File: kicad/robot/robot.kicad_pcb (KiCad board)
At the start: 4 copper layers, 3 parts

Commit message: initial layout work
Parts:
- removed ZZ1: These assemblies are ESD sensitive, ESD precautions shall b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, AltiumImports:AssemblyNote
- removed ZZ2: These assemblies must be clean and free from flux and all c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, AltiumImports:AssemblyNote
- removed ZZ3: These assemblies must comply with workmanship standards IPC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, AltiumImports:AssemblyNote
- added BT1: DNP, custom_modules:battery26650_thermistor, F.Cu at (100.1, 74.9)
- added C1: 100uF, Capacitor_SMD:C_1210_3225Metric, F.Cu at (233.3, 101.4)
- added C10: 1u, Capacitor_SMD:C_0402_1005Metric, F.Cu at (87.9, 139.6)
- added C11: 100n, Capacitor_SMD:C_0402_1005Metric, F.Cu at (79.0, 146.1)
- added C12: 100n, Capacitor_SMD:C_0402_1005Metric, F.Cu at (91.2, 142.5)
- added C13: 100n, Capacitor_SMD:C_0402_1005Metric, F.Cu at (91.2, 146.6)
- added C14: 100n, Capacitor_SMD:C_0402_1005Metric, F.Cu at (84.4, 151.3)
- added C15: 100n, Capacitor_SMD:C_0402_1005Metric, F.Cu at (79.0, 142.5)
- added C16: 100n, Capacitor_SMD:C_0402_1005Metric, F.Cu at (88.9, 139.6)
- added C17: 10u, Capacitor_SMD:C_0603_1608Metric, F.Cu at (78.5, 147.3)
- added C18: 27pF, Capacitor_SMD:C_0402_1005Metric, F.Cu at (128.7, 105.5)
- added C19: 27pF, Capacitor_SMD:C_0402_1005Metric, F.Cu at (128.7, 104.5)
- added C2: 27p, Capacitor_SMD:C_0402_1005Metric, F.Cu at (74.3, 158.3)
- added C20: 2.2uF, Capacitor_SMD:C_0805_2012Metric, F.Cu at (123.2, 108.1)
- added C21: 1uF, Capacitor_SMD:C_0805_2012Metric, F.Cu at (94.7, 98.2)
- added C22: 1uF, Capacitor_SMD:C_0805_2012Metric, F.Cu at (98.2, 100.0)
- added C23: 4.7uF, Capacitor_SMD:C_0805_2012Metric, F.Cu at (101.5, 98.2)
- added C24: 100nF, Capacitor_SMD:C_0603_1608Metric, F.Cu at (80.9, 115.8)
- added C25: 10uF, Capacitor_SMD:C_0805_2012Metric, F.Cu at (86.1, 116.1)
- added C26: 0.47uF, Capacitor_SMD:C_0603_1608Metric, F.Cu at (83.4, 118.0)
- added C27: 10uF, Capacitor_SMD:C_0805_2012Metric, F.Cu at (88.1, 116.1)
- added C28: 2.2uF, Capacitor_SMD:C_0603_1608Metric, F.Cu at (83.4, 122.5)
- added C29: 100nF, Capacitor_SMD:C_0805_2012Metric, F.Cu at (90.2, 116.1)
- added C3: 27p, Capacitor_SMD:C_0402_1005Metric, F.Cu at (82.4, 158.3)
- added C30: 0.22uF, Capacitor_SMD:C_0603_1608Metric, F.Cu at (92.4, 118.9)
- added C31: 0.22uF, Capacitor_SMD:C_0603_1608Metric, F.Cu at (92.4, 121.9)
- added C32: 100nF, Capacitor_SMD:C_0805_2012Metric, F.Cu at (86.1, 124.6)
- added C33: 22uF, Capacitor_SMD:C_0805_2012Metric, F.Cu at (88.1, 124.6)
- added C34: 22uF, Capacitor_SMD:C_0805_2012Metric, F.Cu at (90.2, 124.6)
- added C35: 0.1uF, Capacitor_SMD:C_0603_1608Metric, F.Cu at (96.4, 147.4)
- added C36: 100nF, Capacitor_SMD:C_0603_1608Metric, F.Cu at (91.7, 145.3)
- added C37: 100nF, Capacitor_SMD:C_0603_1608Metric, F.Cu at (94.1, 139.3)
- added C38: 100nF, Capacitor_SMD:C_0603_1608Metric, F.Cu at (101.0, 141.5)
- added C39: 100nF, Capacitor_SMD:C_0603_1608Metric, F.Cu at (101.0, 146.1)
- added C4: 1uF, Capacitor_SMD:C_0603_1608Metric, F.Cu at (64.0, 118.4)
- added C40: 100nF, Capacitor_SMD:C_0805_2012Metric, F.Cu at (120.5, 123.0)
- added C41: 100nF, Capacitor_SMD:C_0805_2012Metric, F.Cu at (131.3, 123.8)
- added C42: 10uF, Capacitor_SMD:C_0805_2012Metric, F.Cu at (120.5, 120.9)
- added C43: 10uF, Capacitor_SMD:C_0805_2012Metric, F.Cu at (131.3, 125.8)
- added C44: 0.1uF, Capacitor_SMD:C_0603_1608Metric, F.Cu at (133.0, 129.9)
- added C45: 27pF, Capacitor_SMD:C_0402_1005Metric, B.Cu at (156.6, 149.4)
- added C46: 27pF, Capacitor_SMD:C_0402_1005Metric, B.Cu at (155.6, 149.4)
- added C47: 1uF, Capacitor_SMD:C_0805_2012Metric, F.Cu at (156.1, 147.5)
- added C48: 1uF, Capacitor_SMD:C_0805_2012Metric, F.Cu at (162.5, 152.4)
- added C49: 2.2uF, Capacitor_SMD:C_0603_1608Metric, F.Cu at (162.3, 154.2)
- added C5: 100n, Capacitor_SMD:C_0402_1005Metric, F.Cu at (80.6, 130.8)
- added C50: 1uF, Capacitor_SMD:C_0805_2012Metric, F.Cu at (159.6, 147.5)
- added C51: 1uF, Capacitor_SMD:C_0603_1608Metric, F.Cu at (154.3, 147.8)
- added C52: 1uF, Capacitor_SMD:C_0603_1608Metric, F.Cu at (157.9, 147.7)
- added C53: 1uF, Capacitor_SMD:C_0603_1608Metric, F.Cu at (149.7, 152.5)
- added C54: 1uF, Capacitor_SMD:C_0603_1608Metric, F.Cu at (149.8, 150.9)
- added C55: 1uF, Capacitor_SMD:C_0603_1608Metric, F.Cu at (66.4, 105.9)
- added C56: 0.47uF, Capacitor_SMD:C_0603_1608Metric, F.Cu at (68.0, 105.9)
- added C57: 0.1uF, Capacitor_SMD:C_0603_1608Metric, F.Cu at (62.9, 103.2)
- added C58: 0.1uF, Capacitor_SMD:C_0603_1608Metric, F.Cu at (62.9, 100.1)
- added C59: 0.1uF, Capacitor_SMD:C_0603_1608Metric, F.Cu at (64.7, 95.8)
- added C6: 100n, Capacitor_SMD:C_0402_1005Metric, F.Cu at (84.9, 139.6)
- added C60: 0.1uF, Capacitor_SMD:C_0603_1608Metric, F.Cu at (67.0, 96.6)
- added C61: 0.1uF, Capacitor_SMD:C_0603_1608Metric, F.Cu at (69.3, 95.8)
- added C62: 0.1uF, Capacitor_SMD:C_0603_1608Metric, F.Cu at (71.0, 93.2)
- added C63: 0.1uF, Capacitor_SMD:C_0603_1608Metric, F.Cu at (72.5, 93.2)
- added C64: 0.1uF, Capacitor_SMD:C_0603_1608Metric, F.Cu at (72.1, 104.2)
- added C65: 0.1uF, Capacitor_SMD:C_0603_1608Metric, F.Cu at (76.0, 96.9)
- added C66: 0.1uF, Capacitor_SMD:C_0603_1608Metric, F.Cu at (76.0, 100.0)
- added C67: 10uF, Capacitor_SMD:C_0805_2012Metric, F.Cu at (123.2, 143.5)
- added C68: 10uF, Capacitor_SMD:C_0805_2012Metric, F.Cu at (123.2, 141.4)
- added C69: 1uF, Capacitor_SMD:C_0603_1608Metric, F.Cu at (118.8, 157.6)
- added C7: 100n, Capacitor_SMD:C_0402_1005Metric, F.Cu at (85.4, 151.3)
- added C70: 100nF, Capacitor_SMD:C_0603_1608Metric, F.Cu at (117.3, 157.6)
- added C71: 100nF, Capacitor_SMD:C_0603_1608Metric, F.Cu at (117.7, 147.6)
- added C72: 100nF, Capacitor_SMD:C_0603_1608Metric, F.Cu at (111.6, 151.9)
- added C73: 100nF, Capacitor_SMD:C_0603_1608Metric, F.Cu at (122.1, 152.5)
- added C74: 100nF, Capacitor_SMD:C_0603_1608Metric, F.Cu at (72.2, 119.9)
- added C75: 10uF, Capacitor_SMD:C_0603_1608Metric, F.Cu at (111.5, 153.5)
- added C76: 22uF, Capacitor_SMD:C_0805_2012Metric, F.Cu at (125.5, 152.3)
- added C77: 10uF, Capacitor_SMD:C_0805_2012Metric, F.Cu at (122.0, 150.6)
- added C78: 22uF, Capacitor_SMD:C_0805_2012Metric, F.Cu at (125.5, 150.2)
- added C8: 1u, Capacitor_SMD:C_0402_1005Metric, F.Cu at (86.9, 139.6)
- added C80: 10uF, Capacitor_SMD:C_0805_2012Metric, F.Cu at (122.0, 148.5)
- added C84: 10nF, Capacitor_SMD:C_0402_1005Metric, F.Cu at (69.3, 121.5)
- added C85: 100nF, Capacitor_SMD:C_0603_1608Metric, F.Cu at (64.0, 121.4)
- added C86: 22uF, Capacitor_SMD:C_0603_1608Metric, F.Cu at (72.2, 121.4)
- added C87: 22uF, Capacitor_SMD:C_0603_1608Metric, F.Cu at (64.0, 119.9)
- added C88: 1uF, Capacitor_SMD:C_0603_1608Metric, F.Cu at (72.0, 114.5)
- added C9: 100n, Capacitor_SMD:C_0402_1005Metric, F.Cu at (86.0, 139.6)
- added C90: 100nF, Capacitor_SMD:C_0603_1608Metric, F.Cu at (72.2, 116.9)
- added C91: 22uF, Capacitor_SMD:C_0603_1608Metric, F.Cu at (72.2, 118.4)
- added C92: 100nF, Capacitor_SMD:C_0603_1608Metric, F.Cu at (70.5, 114.5)
- added C93: 22uF, Capacitor_SMD:C_0603_1608Metric, F.Cu at (69.0, 114.5)
- added C94: 100uF, Capacitor_SMD:C_1210_3225Metric, F.Cu at (125.9, 108.6)
- added D1: AZ23C5V6-7-F, Package_TO_SOT_SMD:Diodes_Inc-SOT23-01_2017-0-MFG, F.Cu at (134.2, 95.1)
- added D2: PTVS20VS1UR, Diode_SMD:Nexperia_CFP3_SOD-123W, F.Cu at (128.7, 108.6)
- added D5: PTVS20VS1UR, Diode_SMD:Nexperia_CFP3_SOD-123W, F.Cu at (123.8, 145.6)
- added D6: LED, Diode_SMD:D_0603_1608Metric_Harvatek, F.Cu at (114.7, 144.5)
- added H1: MountingHole, MountingHole:MountingHole_2.7mm_M2.5, F.Cu at (63.9, 156.4)
- added H2: MountingHole, MountingHole:MountingHole_2.7mm_M2.5, F.Cu at (136.7, 156.4)
- added H3: MountingHole, MountingHole:MountingHole_2.7mm_M2.5, F.Cu at (83.2, 94.5)
- added H4: MountingHole, MountingHole:MountingHole_2.7mm_M2.5, F.Cu at (117.5, 94.9)
- added IN1: TestPoint, TestPoint:KEYSTONE_5002, F.Cu at (83.3, 115.4)
- added J1: USBC_Receptacle_SMD_RA, AltiumImports:CON_USB3.1-C_RCPT_SMD_RA_ACP_12401610E4#2A, F.Cu at (135.8, 105.8)
- added J2: Conn_01x02, Connector_PinHeader_2.54mm:PinHeader_1x02_P2.54mm_Vertical, F.Cu at (79.3, 136.2)
- added J3: 67996-412HLF, Connector_PinHeader_2.54mm:PinHeader_2x06_P2.54mm_Vertical, F.Cu at (124.5, 121.6)
- added JP1: 76VIO, custom_connectors:2.54mm_2pointCurrentTestPoint, F.Cu at (233.1, 94.1)
- added JP2: 58VCIN, custom_connectors:2.54mm_2pointCurrentTestPoint, F.Cu at (156.2, 143.7)
- added JP3: 58SYS, custom_connectors:2.54mm_2pointCurrentTestPoint, F.Cu at (166.3, 148.8)
- added JP4: 58VBUS, custom_connectors:2.54mm_2pointCurrentTestPoint, F.Cu at (162.6, 143.7)
- added JP5: 58VIO2, custom_connectors:2.54mm_2pointCurrentTestPoint, F.Cu at (149.0, 158.2)
- added JP6: 58VIO1, custom_connectors:2.54mm_2pointCurrentTestPoint, F.Cu at (146.9, 145.5)
- added JP7: 76VIO, custom_connectors:2.54mm_2pointCurrentTestPoint, F.Cu at (109.5, 142.0)
- added JP8: 76SUSPND, custom_connectors:2.54mm_2pointCurrentTestPoint, F.Cu at (109.5, 145.7)
- added JP9: 76DISQBAT, custom_connectors:2.54mm_2pointCurrentTestPoint, F.Cu at (109.5, 149.4)
- added L1: 1.5uH, custom_inductors:NRS6028T1R5NMGJ, F.Cu at (96.6, 120.4)
- added L2: 0.47uH, custom_inductors:Vishay-IHLP-2020BZ-FP_1.905x2.79-3D_2.0-0-0-MFG, F.Cu at (124.1, 156.2)
- added L3: 1.5uH, custom_inductors:NRS6028T1R5NMGJ, F.Cu at (66.8, 125.6)
- added OUT1: TestPoint, TestPoint:KEYSTONE_5002, F.Cu at (92.8, 125.5)
- added PGND1: TestPoint, TestPoint:KEYSTONE_5002, F.Cu at (90.7, 128.0)
- added Q2: EFC8811R-TF, custom_transistors:ON_Semiconductor-568AL-10_2013-O-MFG, F.Cu at (71.3, 97.5)
- added R1: 1k, Resistor_SMD:R_0402_1005Metric, F.Cu at (80.2, 138.6)
- added R10: 1k, Resistor_SMD:R_0603_1608Metric, F.Cu at (133.2, 91.8)
- added R11: 1k, Resistor_SMD:R_0603_1608Metric, F.Cu at (134.7, 91.8)
- added R12: 100, Resistor_SMD:R_0603_1608Metric, F.Cu at (137.1, 91.0)
- added R13: 100, Resistor_SMD:R_0603_1608Metric, F.Cu at (137.1, 92.5)
- added R14: 1k, Resistor_SMD:R_0603_1608Metric, F.Cu at (136.6, 95.1)
- added R15: 1k, Resistor_SMD:R_0603_1608Metric, F.Cu at (138.1, 95.1)
- added R16: 510k, Resistor_SMD:R_0603_1608Metric, F.Cu at (96.6, 94.8)
- added R17: 100k, Resistor_SMD:R_0603_1608Metric, F.Cu at (99.6, 94.8)
- added R18: 47K, Resistor_SMD:R_0603_1608Metric, F.Cu at (103.4, 94.8)
- added R19: 200k, Resistor_SMD:R_0603_1608Metric, F.Cu at (79.4, 115.8)
- added R2: DNF, Resistor_SMD:R_0402_1005Metric, F.Cu at (79.6, 130.8)
- added R20: 2.2k, Resistor_SMD:R_0603_1608Metric, F.Cu at (83.4, 121.0)
- added R21: 2.2k, Resistor_SMD:R_0603_1608Metric, F.Cu at (83.4, 119.5)
- added R22: 100, Resistor_SMD:R_0603_1608Metric, F.Cu at (91.7, 143.8)
- added R23: 100, Resistor_SMD:R_0603_1608Metric, F.Cu at (95.6, 139.3)
- added R24: 100, Resistor_SMD:R_0603_1608Metric, F.Cu at (101.0, 143.0)
- added R25: 100, Resistor_SMD:R_0603_1608Metric, F.Cu at (101.0, 144.5)
- added R26: DNP, Resistor_SMD:R_0603_1608Metric, F.Cu at (120.2, 126.3)
- added R27: DNP, Resistor_SMD:R_0603_1608Metric, F.Cu at (131.5, 122.0)
- added R28: 10k, Resistor_SMD:R_0603_1608Metric, F.Cu at (115.6, 120.7)
- added R29: 0.4, Resistor_SMD:R_0603_1608Metric, F.Cu at (120.2, 124.8)
- added R3: 27, Resistor_SMD:R_0402_1005Metric, F.Cu at (91.2, 141.4)
- added R30: 0.4, Resistor_SMD:R_0603_1608Metric, F.Cu at (131.5, 120.5)
- added R31: 10k, Resistor_SMD:R_0603_1608Metric, F.Cu at (136.2, 126.3)
- added R32: 1, Resistor_SMD:R_0402_1005Metric, B.Cu at (153.2, 152.5)
- added R33: 1, Resistor_SMD:R_0402_1005Metric, B.Cu at (153.2, 151.5)
- added R34: 2.2k, Resistor_SMD:R_0603_1608Metric, F.Cu at (149.7, 154.0)
- added R35: 2.2k, Resistor_SMD:R_0603_1608Metric, F.Cu at (149.7, 155.5)
- added R36: 200k, Resistor_SMD:R_0603_1608Metric, F.Cu at (152.8, 147.8)
- added R37: 649k, Resistor_SMD:R_0603_1608Metric, F.Cu at (159.8, 156.7)
- added R38: 120k, Resistor_SMD:R_0603_1608Metric, F.Cu at (158.3, 156.7)
- added R39: 649k, Resistor_SMD:R_0603_1608Metric, F.Cu at (162.3, 150.4)
- added R4: 27, Resistor_SMD:R_0402_1005Metric, F.Cu at (91.2, 140.4)
- added R40: 120k, Resistor_SMD:R_0603_1608Metric, F.Cu at (162.3, 148.9)
- added R41: 10, Resistor_SMD:R_0603_1608Metric, F.Cu at (62.9, 98.6)
- added R42: 10, Resistor_SMD:R_0603_1608Metric, F.Cu at (62.9, 101.7)
- added R43: 200, Resistor_SMD:R_0603_1608Metric, F.Cu at (66.2, 94.3)
- added R44: 5m, Resistor_SMD:R_0603_1608Metric, F.Cu at (67.0, 92.0)
- added R45: 200, Resistor_SMD:R_0603_1608Metric, F.Cu at (67.8, 94.3)
- added R46: 1k, Resistor_SMD:R_0603_1608Metric, F.Cu at (70.6, 101.2)
- added R47: 1k, Resistor_SMD:R_0603_1608Metric, F.Cu at (73.6, 101.2)
- added R48: 2k, Resistor_SMD:R_0603_1608Metric, F.Cu at (72.1, 101.2)
- added R49: 100k, Resistor_SMD:R_0603_1608Metric, F.Cu at (114.6, 147.6)
- added R5: 1k, Resistor_SMD:R_0402_1005Metric, F.Cu at (82.9, 151.3)
- added R50: 1k, Resistor_SMD:R_0603_1608Metric, F.Cu at (119.2, 147.6)
- added R52: 768k, Resistor_SMD:R_0603_1608Metric, F.Cu at (66.0, 114.5)
- added R53: 113K, Resistor_SMD:R_0603_1608Metric, F.Cu at (67.5, 114.5)
- added R54: 28k, Resistor_SMD:R_0603_1608Metric, F.Cu at (64.0, 116.9)
- added R55: 14k, Resistor_SMD:R_0603_1608Metric, F.Cu at (64.4, 114.5)
- added R56: 10, Resistor_SMD:R_0603_1608Metric, F.Cu at (116.1, 147.6)
- added R6: 0, Resistor_SMD:R_0603_1608Metric, F.Cu at (130.1, 95.1)
- added R7: 0, Resistor_SMD:R_0603_1608Metric, F.Cu at (131.6, 95.1)
- added R8: 100, Resistor_SMD:R_0603_1608Metric, F.Cu at (130.8, 91.0)
- added R9: 100, Resistor_SMD:R_0603_1608Metric, F.Cu at (130.8, 92.5)
- added SCL1V1: TestPoint, TestPoint:KEYSTONE_5002, F.Cu at (80.0, 124.9)
- added SDA1V1: TestPoint, TestPoint:KEYSTONE_5002, F.Cu at (83.2, 124.9)
- added TP12: SWD, TestPoint:TestPoint_2Pads_Pitch2mm_SMD, F.Cu at (119.2, 144.8)
- added TP16: TestPoint, TestPoint:KEYSTONE_5002, F.Cu at (152.9, 154.7)
- added TP17: TestPoint, TestPoint:KEYSTONE_5002, F.Cu at (155.8, 156.2)
- added TP18: TestPoint, TestPoint:KEYSTONE_5002, F.Cu at (155.8, 140.1)
- added TP19: TestPoint, TestPoint:KEYSTONE_5002, F.Cu at (159.0, 140.1)
- added TP20: TestPoint, TestPoint:KEYSTONE_5002, F.Cu at (150.5, 148.4)
- added TP21: TestPoint, TestPoint:KEYSTONE_5002, F.Cu at (146.7, 154.8)
- added TP22: TestPoint, TestPoint:KEYSTONE_5002, F.Cu at (150.5, 145.1)
- added TP23: TestPoint, TestPoint:KEYSTONE_5002, F.Cu at (119.4, 141.7)
- added TP24: TestPoint, TestPoint:KEYSTONE_5002, F.Cu at (113.6, 155.8)
- added TP25: TestPoint, TestPoint:KEYSTONE_5002, F.Cu at (128.8, 151.3)
- added TP26: TestPoint, TestPoint:KEYSTONE_5002, F.Cu at (128.8, 148.0)
- added TP27: SWD, custom_connectors:2.54mm_2pointCurrentTestPoint, F.Cu at (87.8, 152.4)
- added TP28: SWD, TestPoint:TestPoint_2Pads_Pitch2mm_SMD, F.Cu at (90.8, 152.2)
- added U1: WRM483265-10F5-12V-G, custom_modules:WRM483265-10F5-12V-G, F.Cu at (232.4, 87.7)
- added U10: SN74AHC125RGYR, Ultra_Librarian:SN74AHC125RGYR, F.Cu at (133.0, 133.7)
- added U11: MAX77958EWV+T, Ultra_Librarian:MAX77958EWV&plus_T, F.Cu at (156.1, 152.0)
- added U12: BQ27742YZFR-G1, Package_BGA:Texas_Instruments-YZF0015-0-0-MFG, F.Cu at (67.2, 100.9)
- added U13: MAX77976EFD+, Ultra_Librarian:MAX77976, F.Cu at (117.3, 152.5)
- added U14: MAX77642ANA+, Package_BGA:Maxim-N252B2-1-0-A-MFG, F.Cu at (68.1, 118.7)
- added U15: ESD122DMYR, Diode_SMD:Texas_Instruments-DMY0003A-0-0-MFG, B.Cu at (151.5, 152.0)
- added U2: W25Q128JVS, Package_SO:SOIC-8_5.23x5.23mm_P1.27mm, F.Cu at (84.1, 133.9)
- added U3: RP2040, RP2040_minimal:RP2040-QFN-56, F.Cu at (85.1, 145.1)
- added U4: NCP3901, custom_modules:NCP3901, F.Cu at (98.1, 97.4)
- added U5: LSF0102DCTR, Snapeda:SOP65P400X130-8N, F.Cu at (80.1, 120.3)
- added U6: MAX77857, Package_BGA:WLP-35_7x5_2.828x2.028mm, F.Cu at (88.1, 120.4)
- added U7: SN74AHC125RGYR, Ultra_Librarian:SN74AHC125RGYR, F.Cu at (96.4, 143.8)
- added U8: DRV8830DRCR, Snapeda:IC_DRV8830DRCR, F.Cu at (116.1, 123.9)
- added U9: DRV8830DRCR, Snapeda:IC_DRV8830DRCR, F.Cu at (135.7, 122.9)
- added Y1: ABLS-12.000MHZ-B4-T, RP2040_minimal:Crystal_SMD_HC49-US, F.Cu at (78.4, 155.1)
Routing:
- net /SYS: track 0.00 -> 27.7 mm, vias 0 -> 2
- net /3V3: track 0.00 -> 25.9 mm
- net /MCU/GPIO26_ADC0: track 0.00 -> 19.3 mm, vias 0 -> 2
- net /USB-PD/VIO1_: track 0.00 -> 18.1 mm
- net /MCU/XIN: track 0.00 -> 17.6 mm
- net /MCU/GPIO27_ADC1: track 0.00 -> 16.2 mm, vias 0 -> 2
- net /MCU/GPIO28_ADC2: track 0.00 -> 16.2 mm, vias 0 -> 2
- net /MCU/QSPI_SD0: track 0.00 -> 15.5 mm, vias 0 -> 2
- net /MCU/QSPI_SS: track 0.00 -> 13.8 mm
- net /MCU/QSPI_SD3: track 0.00 -> 13.6 mm, vias 0 -> 2
- net /USB-PD/VIO2_: track 0.00 -> 13.5 mm
- net /1V8: track 0.00 -> 11.8 mm
- net Net-(R21-Pad2): track 0.00 -> 11.7 mm, vias 0 -> 2
- net Net-(C71-Pad1): track 0.00 -> 11.7 mm
- net /MCU/QSPI_SCLK: track 0.00 -> 11.6 mm, vias 0 -> 2
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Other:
- board outline added: 80 x 100 mm

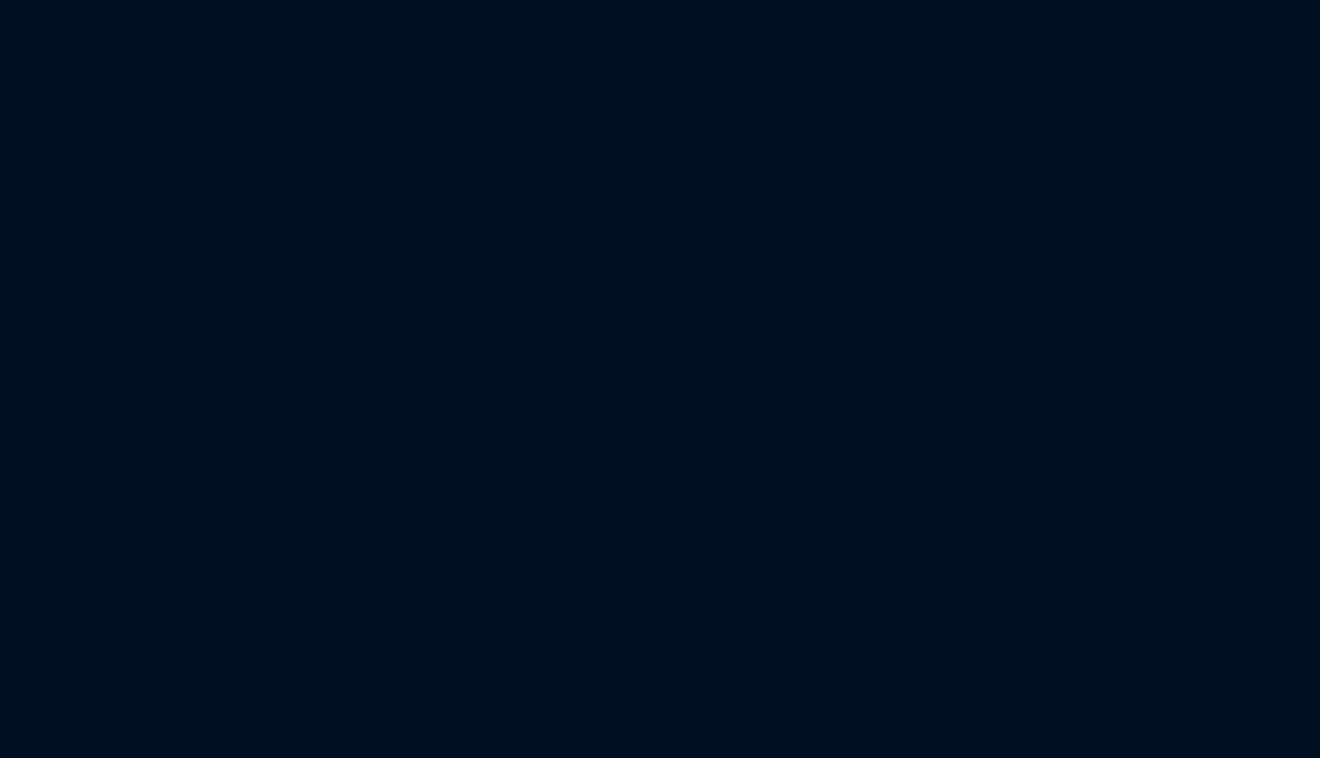
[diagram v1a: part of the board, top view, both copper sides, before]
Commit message: Updated PCB with new parts
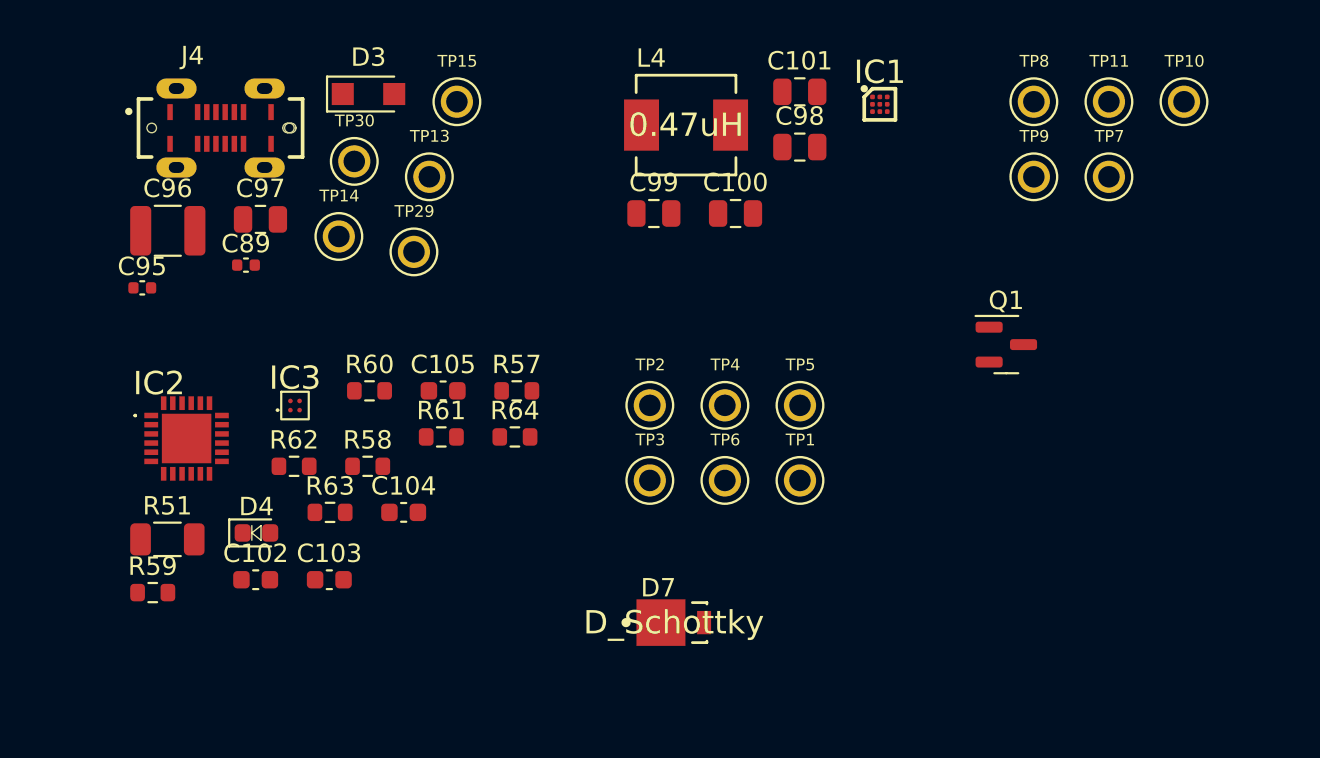
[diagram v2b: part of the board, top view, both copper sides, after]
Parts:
- added C100: 10uF, Capacitor_SMD:C_0805_2012Metric, F.Cu at (193.3, 52.1)
- added C101: 4.7uF, Capacitor_SMD:C_0805_2012Metric, F.Cu at (196.8, 45.5)
- added C102: 0.1uF, Capacitor_SMD:C_0603_1608Metric, F.Cu at (167.2, 72.1)
- added C103: 0.1uF, Capacitor_SMD:C_0603_1608Metric, F.Cu at (171.2, 72.1)
- added C104: 0.1uF, Capacitor_SMD:C_0603_1608Metric, F.Cu at (175.3, 68.4)
- added C105: 1uF, Capacitor_SMD:C_0603_1608Metric, F.Cu at (177.4, 61.8)
- added C89: 27pF, Capacitor_SMD:C_0402_1005Metric, F.Cu at (166.7, 54.9)
- added C95: 27pF, Capacitor_SMD:C_0402_1005Metric, F.Cu at (161.0, 56.2)
- added C96: 100uF, Capacitor_SMD:C_1210_3225Metric, F.Cu at (162.4, 53.0)
- added C97: 2.2uF, Capacitor_SMD:C_0805_2012Metric, F.Cu at (167.5, 52.4)
- added C98: 4.7uF, Capacitor_SMD:C_0805_2012Metric, F.Cu at (196.8, 48.5)
- added C99: 4.7uF, Capacitor_SMD:C_0805_2012Metric, F.Cu at (188.9, 52.1)
- added D3: PTVS20VS1UR, Diode_SMD:Nexperia_CFP3_SOD-123W, F.Cu at (173.4, 45.6)
- added D4: LED, Diode_SMD:D_0603_1608Metric_Harvatek, F.Cu at (167.2, 69.5)
- added D7: D_Schottky, Diode_SMD:Vishay-SS1P3L-M3_84A-0-0-0, F.Cu at (190.0, 74.4)
- added IC1: TPS61253AYFFR, Package_BGA:Texas_Instruments-YFF0009-BGA9C40P3X3_119X129X62, F.Cu at (201.2, 46.2)
- added IC2: AP33771DKZ-13, Package_DFN_QFN:AP33771DKZ13, F.Cu at (163.4, 64.4)
- added IC3: EFC4626R-TR, Package_BGA:ON_SEMI_EFCP1010-4DG-020, F.Cu at (169.3, 62.6)
- added J4: USB4120-03-C_REVA, Connector_USB:GCT_USB4120-03-C_REVA, F.Cu at (165.3, 47.5)
- added L4: 0.47uH, custom_inductors:Vishay-IHLP-2020BZ-FP_1.905x2.79-3D_2.0-0-0-MFG, F.Cu at (190.7, 47.3)
- added Q1: Q_NMOS_GDS, Package_TO_SOT_SMD:SOT-23, F.Cu at (208.1, 59.2)
- added R51: 10m, Resistor_SMD:R_1206_3216Metric, F.Cu at (162.4, 69.9)
- added R57: 10k, Resistor_SMD:R_0603_1608Metric, F.Cu at (181.4, 61.8)
- added R58: 100, Resistor_SMD:R_0603_1608Metric, F.Cu at (173.3, 65.9)
- added R59: 100k, Resistor_SMD:R_0603_1608Metric, F.Cu at (161.6, 72.8)
- added R60: 100k, Resistor_SMD:R_0603_1608Metric, F.Cu at (173.4, 61.8)
- added R61: 100k, Resistor_SMD:R_0603_1608Metric, F.Cu at (177.3, 64.3)
- added R62: 16k, Resistor_SMD:R_0603_1608Metric, F.Cu at (169.3, 65.9)
- added R63: 5.1k, Resistor_SMD:R_0603_1608Metric, F.Cu at (171.3, 68.4)
- added R64: 5.1k, Resistor_SMD:R_0603_1608Metric, F.Cu at (181.3, 64.3)
- added TP1: SDA_SL, TestPoint:KEYSTONE_5002, F.Cu at (196.9, 66.7)
- added TP10: CC2, TestPoint:KEYSTONE_5002, F.Cu at (217.8, 46.0)
- added TP11: VBUS, TestPoint:KEYSTONE_5002, F.Cu at (213.7, 46.0)
- added TP13: D-, TestPoint:KEYSTONE_5002, F.Cu at (176.7, 50.1)
- added TP14: D+, TestPoint:KEYSTONE_5002, F.Cu at (171.7, 53.4)
- added TP15: CC1, TestPoint:KEYSTONE_5002, F.Cu at (178.2, 46.0)
- added TP2: SCL_SL, TestPoint:KEYSTONE_5002, F.Cu at (188.7, 62.6)
- added TP29: CC2, TestPoint:KEYSTONE_5002, F.Cu at (175.8, 54.2)
- added TP3: I2C0_SDA, TestPoint:KEYSTONE_5002, F.Cu at (188.7, 66.7)
- added TP30: VBUS, TestPoint:KEYSTONE_5002, F.Cu at (172.6, 49.3)
- added TP4: I2C0_SCL, TestPoint:KEYSTONE_5002, F.Cu at (192.8, 62.6)
- added TP5: SDA_EXT, TestPoint:KEYSTONE_5002, F.Cu at (196.9, 62.6)
- added TP6: SCL_EXT, TestPoint:KEYSTONE_5002, F.Cu at (192.8, 66.7)
- added TP7: D-, TestPoint:KEYSTONE_5002, F.Cu at (213.7, 50.1)
- added TP8: D+, TestPoint:KEYSTONE_5002, F.Cu at (209.6, 46.0)
- added TP9: CC1, TestPoint:KEYSTONE_5002, F.Cu at (209.6, 50.1)
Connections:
- net /AGND renamed GND
- net /MCU/USB_D+ renamed /MCU/D+
- net /MCU/USB_D- renamed /MCU/D-
- net /USB-PD/DN1 renamed /USB-PD-PhonePC/DN1
- net /USB-PD/DP2 renamed /USB-PD-PhonePC/DP2
- net /USB-PD/GPIO0 renamed /USB-PD-PhonePC/GPIO0
- net /USB-PD/GPIO1 renamed /USB-PD-PhonePC/GPIO1
- net /USB-PD/GPIO3 renamed /USB-PD-PhonePC/GPIO3
- net /USB-PD/VIO1 renamed /USB-PD-PhonePC/VIO1
- net /USB-PD/VIO1_ renamed /USB-PD-PhonePC/VIO1_
- net /USB-PD/VIO2_ renamed /USB-PD-PhonePC/VIO2_
- C18 pad 1: /USB-C/CC1 -> /USB-C_ExtChg/CC1
- C19 pad 1: /USB-C/CC2 -> /USB-C_ExtChg/CC2
- C20 pad 1: /PowerMux/VIN_A -> /USB-C_ExtChg/VBUS
- C45 pad 1: /USB-C/CC2 -> /USB-C_PhonePC/CC2
- C46 pad 1: /USB-C/CC1 -> /USB-C_PhonePC/CC1
- C94 pad 1: /PowerMux/VIN_A -> /USB-C_ExtChg/VBUS
- D2 pad 1: /PowerMux/VIN_A -> /USB-C_ExtChg/VBUS
- J1 pad A4: /PowerMux/VIN_A -> /USB-C_ExtChg/VBUS
- J1 pad A5: /USB-C/CC1 -> /USB-C_ExtChg/CC1
- J1 pad A6: /USB-C/D+ -> /USB-C_ExtChg/D+
- J1 pad A7: /USB-C/D- -> /USB-C_ExtChg/D-
- J1 pad A8: /USB-C/SBU1 -> unconnected-(J1-PadA8)
- J1 pad A9: /PowerMux/VIN_A -> /USB-C_ExtChg/VBUS
- J1 pad B4: /PowerMux/VIN_A -> /USB-C_ExtChg/VBUS
- J1 pad B5: /USB-C/CC2 -> /USB-C_ExtChg/CC2
- J1 pad B6: /USB-C/D+ -> /USB-C_ExtChg/D+
- J1 pad B7: /USB-C/D- -> /USB-C_ExtChg/D-
- J1 pad B8: /USB-C/SBU2 -> unconnected-(J1-PadB8)
- J1 pad B9: /PowerMux/VIN_A -> /USB-C_ExtChg/VBUS
- JP4 pad 1: /PowerMux/VIN_A -> /USB-C_PhonePC/VBUS
- R32 pad 1: /USB-C/D- -> /USB-C_PhonePC/D+
- R33 pad 1: /USB-C/D+ -> /USB-C_PhonePC/D-
- R38 pad 2: /USB-C/SBU1 -> /USB-C_PhonePC/SBU1
- R40 pad 2: /USB-C/SBU2 -> /USB-C_PhonePC/SBU2
- U11 pad A3: /USB-C/CC1 -> /USB-C_PhonePC/CC1
- U11 pad A4: /USB-C/CC2 -> /USB-C_PhonePC/CC2
- U15 pad 2: /USB-C/D+ -> /USB-C_PhonePC/D-
- U15 pad 3: /USB-C/D- -> /USB-C_PhonePC/D+
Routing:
- net /USB-C_PhonePC/D+: track 0.00 -> 1.04 mm
- net /USB-C/D-: track 1.04 -> 0.00 mm
- net /USB-C_PhonePC/D-: track 0.00 -> 1.04 mm
- net /USB-C/D+: track 1.04 -> 0.00 mm
